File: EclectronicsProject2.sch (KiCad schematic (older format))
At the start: 84 parts, among them J7 Barrel_Jack, U11 TPS62290DRVR, U8 TPS62290DRVR

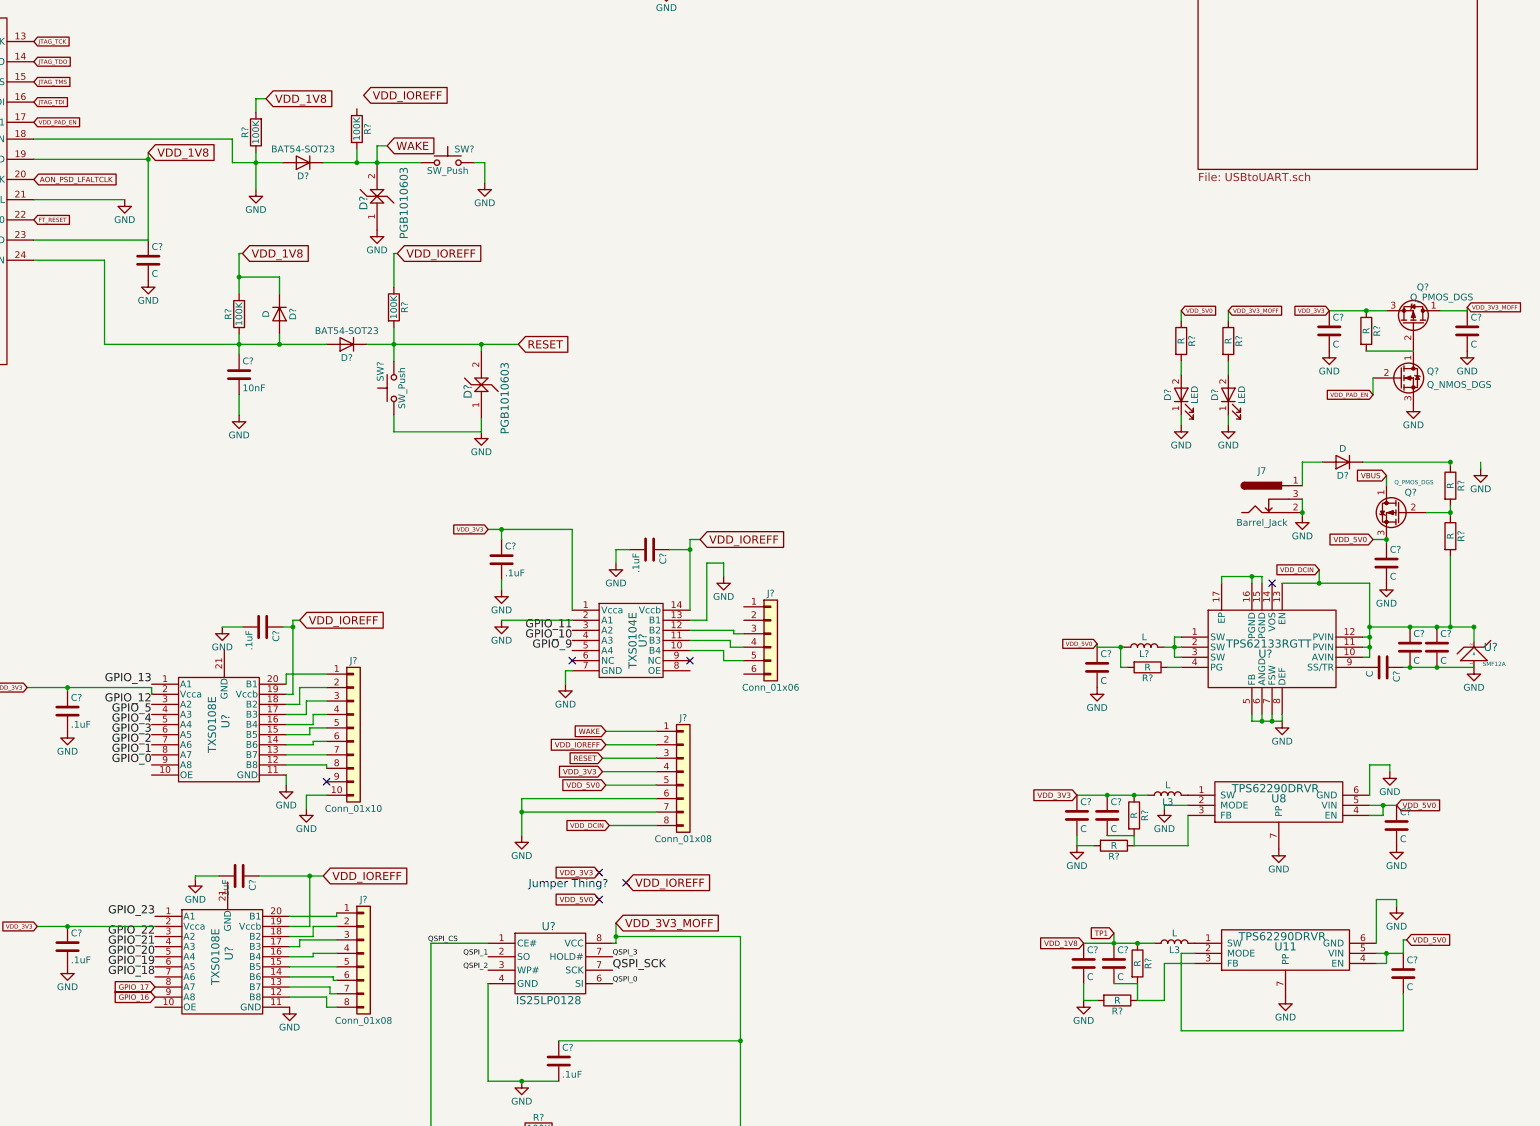
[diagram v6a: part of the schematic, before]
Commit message: adding some of the component labels
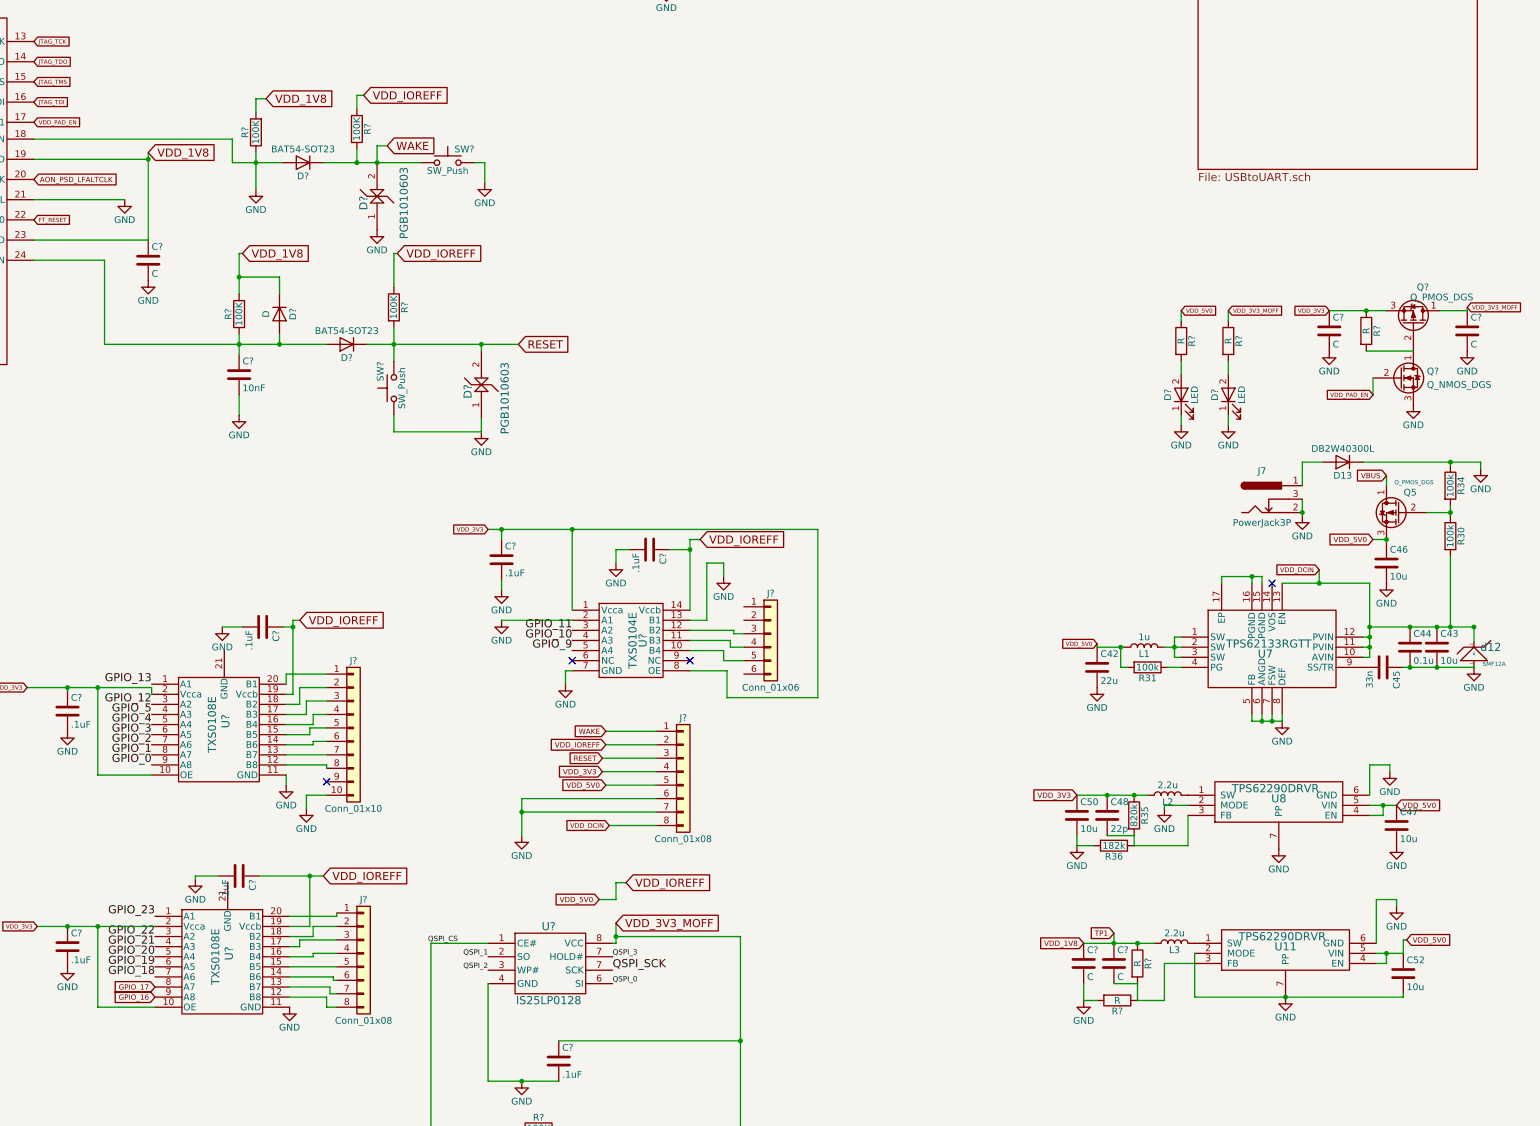
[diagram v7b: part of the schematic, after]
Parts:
- C42: renamed from C?; value C -> 22u
- C43, C46, C47, C50, C52: renamed from C?; value C -> 10u
- C44: renamed from C?; value C -> 0.1u
- C45: renamed from C?; value C -> 33n
- C48: renamed from C?; value C -> 22p
- D13: renamed from D?; value D -> DB2W40300L
- J7: value Barrel_Jack -> PowerJack3P
- L1: renamed from L?; value L -> 1u
- L2: renamed from L3; value L -> 2.2u
- L3: value L -> 2.2u
- R30, R31, R34: renamed from R?; value R -> 100k
- R35: renamed from R?; value R -> 820k
- R36: renamed from R?; value R -> 182k
- U7: renamed from U?; PART (none) -> 296-30225-1-ND
- gave numbers to parts that had none: 2
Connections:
- net VDD_IOREFF is gone; now on net VDD_5V0: C?.1, C?.1, C?.1, J?.2 (Pin_2), R?.1, U?.14 (Vccb), U?.19 (Vccb), U?.19 (Vccb)
- net GND: now also C52.2, D13.1 (K), R34.1, U11.2 (MODE)
- net VDD_3V3: now also U?.10 (OE), U?.10 (OE), U?.8 (OE)
- net VDD_5V0: now also R?.1
- no-connect marks 8 -> 5
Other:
- note removed: "Jumper Thing?\n"
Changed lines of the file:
@@
 IVDD
 $Comp
-L C C?
+L C C52
 U 1 1 59CDA679
 P 15725 8800
-F 0 "C?" H 15750 8900 50  0000 L CNN
-F 1 "C" H 15750 8700 50  0000 L CNN
+F 0 "C52" H 15750 8900 50  0000 L CNN
+F 1 "10u" H 15750 8700 50  0000 L CNN
 F 2 "" H 15763 8650 50  0001 C CNN
 F 3 "" H 15725 8800 50  0001 C CNN
@@
 P 14025 8575
 F 0 "L3" V 13975 8575 50  0000 C CNN
-F 1 "L" V 14100 8575 50  0000 C CNN
+F 1 "2.2u" V 14100 8575 50  0000 C CNN
 F 2 "" H 14025 8575 50  0001 C CNN
 F 3 "" H 14025 8575 50  0001 C CNN
@@
 $Comp
 L GND #PWR?
-U 1 1 59CE4525
-P 14850 8975
-F 0 "#PWR?" H 14850 8725 50  0001 C CNN
-F 1 "GND" H 14850 8825 50  0000 C CNN
-F 2 "" H 14850 8975 50  0001 C CNN
-F 3 "" H 14850 8975 50  0001 C CNN
-	1    14850 8975
-	1    0    0    -1
-$EndComp
-$Comp
-L GND #PWR?
 U 1 1 59CE4599
 P 15675 8300
@@
 $EndComp
 $Comp
-L C C?
+L C C47
 U 1 1 59CE5977
 P 15675 7700
-F 0 "C?" H 15700 7800 50  0000 L CNN
-F 1 "C" H 15700 7600 50  0000 L CNN
+F 0 "C47" H 15700 7800 50  0000 L CNN
+F 1 "10u" H 15700 7600 50  0000 L CNN
 F 2 "" H 15713 7550 50  0001 C CNN
 F 3 "" H 15675 7700 50  0001 C CNN
@@
 $EndComp
 $Comp
-L L L3
+L L L2
 U 1 1 59CE66A1
 P 13975 7475
-F 0 "L3" V 13925 7475 50  0000 C CNN
-F 1 "L" V 14050 7475 50  0000 C CNN
+F 0 "L2" V 13925 7475 50  0000 C CNN
+F 1 "2.2u" V 14050 7475 50  0000 C CNN
 F 2 "" H 13975 7475 50  0001 C CNN
 F 3 "" H 13975 7475 50  0001 C CNN
@@
 $EndComp
 $Comp
-L R R?
+L R R35
 U 1 1 59CE674E
 P 13725 7625
-F 0 "R?" V 13805 7625 50  0000 C CNN
-F 1 "R" V 13725 7625 50  0000 C CNN
+F 0 "R35" V 13805 7625 50  0000 C CNN
+F 1 "820k" V 13725 7625 50  0000 C CNN
 F 2 "" V 13655 7625 50  0001 C CNN
 F 3 "" H 13725 7625 50  0001 C CNN
@@
 $EndComp
 $Comp
-L C C?
+L C C48
 U 1 1 59CE6957
 P 13525 7625
-F 0 "C?" H 13550 7725 50  0000 L CNN
-F 1 "C" H 13550 7525 50  0000 L CNN
+F 0 "C48" H 13550 7725 50  0000 L CNN
+F 1 "22p" H 13550 7525 50  0000 L CNN
 F 2 "" H 13563 7475 50  0001 C CNN
 F 3 "" H 13525 7625 50  0001 C CNN
@@
 $EndComp
 $Comp
-L C C?
+L C C50
 U 1 1 59CE6FC0
 P 13300 7625
-F 0 "C?" H 13325 7725 50  0000 L CNN
-F 1 "C" H 13325 7525 50  0000 L CNN
+F 0 "C50" H 13325 7725 50  0000 L CNN
+F 1 "10u" H 13325 7525 50  0000 L CNN
 F 2 "" H 13338 7475 50  0001 C CNN
 F 3 "" H 13300 7625 50  0001 C CNN
@@
 $EndComp
 $Comp
-L R R?
+L R R36
 U 1 1 59CE7280
 P 13575 7850
-F 0 "R?" V 13655 7850 50  0000 C CNN
-F 1 "R" V 13575 7850 50  0000 C CNN
+F 0 "R36" V 13655 7850 50  0000 C CNN
+F 1 "182k" V 13575 7850 50  0000 C CNN
 F 2 "" V 13505 7850 50  0001 C CNN
 F 3 "" H 13575 7850 50  0001 C CNN
@@
 TP1
 $Comp
-L TPS62133RGTT U?
+L TPS62133RGTT U7
 U 1 1 59CD9E4B
 P 14700 6475
-F 0 "U?" H 14700 6525 60  0000 C CNN
+F 0 "U7" H 14700 6525 60  0000 C CNN
 F 1 "TPS62133RGTT" H 14725 6600 60  0000 C CNN
 F 2 "" H 14700 6475 60  0001 C CNN
 F 3 "" H 14700 6475 60  0001 C CNN
+F 4 "296-30225-1-ND" H 14700 6475 60  0001 C CNN "PART"
 	1    14700 6475
 	1    0    0    -1
@@
 $EndComp
 $Comp
-L C C?
+L C C45
 U 1 1 59CDAB83
 P 15575 6525
-F 0 "C?" H 15600 6625 50  0000 L CNN
-F 1 "C" H 15600 6425 50  0000 L CNN
+F 0 "C45" H 15600 6625 50  0000 L CNN
+F 1 "33n" H 15600 6425 50  0000 L CNN
 F 2 "" H 15613 6375 50  0001 C CNN
 F 3 "" H 15575 6525 50  0001 C CNN
@@
 $EndComp
 $Comp
-L C C?
+L C C44
 U 1 1 59CDAC24
 P 15775 6375
-F 0 "C?" H 15800 6475 50  0000 L CNN
-F 1 "C" H 15800 6275 50  0000 L CNN
+F 0 "C44" H 15800 6475 50  0000 L CNN
+F 1 "0.1u" H 15800 6275 50  0000 L CNN
 F 2 "" H 15813 6225 50  0001 C CNN
 F 3 "" H 15775 6375 50  0001 C CNN
@@
 $EndComp
 $Comp
-L C C?
+L C C43
 U 1 1 59CDACF5
 P 15975 6375
-F 0 "C?" H 16000 6475 50  0000 L CNN
-F 1 "C" H 16000 6275 50  0000 L CNN
+F 0 "C43" H 16000 6475 50  0000 L CNN
+F 1 "10u" H 16000 6275 50  0000 L CNN
 F 2 "" H 16013 6225 50  0001 C CNN
 F 3 "" H 15975 6375 50  0001 C CNN
@@
 $EndComp
 $Comp
-L SMF12A U?
+L SMF12A d12
 U 1 1 59CDB688
 P 16350 6425
-F 0 "U?" H 16375 6475 60  0000 C CNN
+F 0 "d12" H 16375 6475 60  0000 C CNN
 F 1 "SMF12A" H 16400 6350 31  0000 C CNN
 F 2 "" H 16150 6375 60  0001 C CNN
@@
 $EndComp
 $Comp
-L R R?
+L R R30
 U 1 1 59CDE56A
 P 16075 5550
-F 0 "R?" V 16155 5550 50  0000 C CNN
-F 1 "R" V 16075 5550 50  0000 C CNN
+F 0 "R30" V 16155 5550 50  0000 C CNN
+F 1 "100k" V 16075 5550 50  0000 C CNN
 F 2 "" V 16005 5550 50  0001 C CNN
 F 3 "" H 16075 5550 50  0001 C CNN
@@
 $EndComp
 $Comp
-L R R?
+L R R34
 U 1 1 59CDE6A4
 P 16075 5175
-F 0 "R?" V 16155 5175 50  0000 C CNN
-F 1 "R" V 16075 5175 50  0000 C CNN
+F 0 "R34" V 16155 5175 50  0000 C CNN
+F 1 "100k" V 16075 5175 50  0000 C CNN
 F 2 "" V 16005 5175 50  0001 C CNN
 F 3 "" H 16075 5175 50  0001 C CNN
@@
 $EndComp
 $Comp
-L Q_PMOS_DGS Q?
+L Q_PMOS_DGS Q5
 U 1 1 59CDFA93
 P 15700 5375
-F 0 "Q?" H 15575 5525 50  0000 L CNN
+F 0 "Q5" H 15575 5525 50  0000 L CNN
 F 1 "Q_PMOS_DGS" H 15450 5600 31  0000 L CNN
 F 2 "" H 15900 5475 50  0001 C CNN
@@
 $EndComp
 $Comp
-L C C?
+L C C46
 U 1 1 59CE0B13
 P 15600 5750
-F 0 "C?" H 15625 5850 50  0000 L CNN
-F 1 "C" H 15625 5650 50  0000 L CNN
+F 0 "C46" H 15625 5850 50  0000 L CNN
+F 1 "10u" H 15625 5650 50  0000 L CNN
 F 2 "" H 15638 5600 50  0001 C CNN
 F 3 "" H 15600 5750 50  0001 C CNN
@@
 P 14675 5275
 F 0 "J7" H 14675 5485 50  0000 C CNN
-F 1 "Barrel_Jack" H 14675 5100 50  0000 C CNN
+F 1 "PowerJack3P" H 14675 5100 50  0000 C CNN
 F 2 "" H 14725 5235 50  0001 C CNN
 F 3 "" H 14725 5235 50  0001 C CNN
@@
 $EndComp
 $Comp
-L L L?
+L L L1
 U 1 1 59CF21B5
 P 13800 6375
-F 0 "L?" V 13750 6375 50  0000 C CNN
-F 1 "L" V 13875 6375 50  0000 C CNN
+F 0 "L1" V 13750 6375 50  0000 C CNN
+F 1 "1u" V 13875 6375 50  0000 C CNN
 F 2 "" H 13800 6375 50  0001 C CNN
 F 3 "" H 13800 6375 50  0001 C CNN
@@
 $EndComp
 $Comp
-L R R?
-U 1 1 59CF2367
-P 13825 6525
-F 0 "R?" V 13905 6525 50  0000 C CNN
-F 1 "R" V 13825 6525 50  0000 C CNN
-F 2 "" V 13755 6525 50  0001 C CNN
-F 3 "" H 13825 6525 50  0001 C CNN
-	1    13825 6525
-	0    1    1    0
-$EndComp
-$Comp
-L C C?
+L C C42
 U 1 1 59CF2896
 P 13450 6525
-F 0 "C?" H 13475 6625 50  0000 L CNN
-F 1 "C" H 13475 6425 50  0000 L CNN
+F 0 "C42" H 13475 6625 50  0000 L CNN
+F 1 "22u" H 13475 6425 50  0000 L CNN
 F 2 "" H 13488 6375 50  0001 C CNN
 F 3 "" H 13450 6525 50  0001 C CNN
@@
 VDD_DCIN
 $Comp
-L D D?
+L D D13
 U 1 1 59CE7139
 P 15275 5000
-F 0 "D?" H 15275 5100 50  0000 C CNN
-F 1 "D" H 15275 4900 50  0000 C CNN
+F 0 "D13" H 15275 5100 50  0000 C CNN
+F 1 "DB2W40300L" H 15275 4900 50  0000 C CNN
 F 2 "" H 15275 5000 50  0001 C CNN
 F 3 "" H 15275 5000 50  0001 C CNN
@@
 	14175 8725 13950 8725
 Wire Wire Line
-	15725 9225 15725 8950
-Wire Wire Line
-	14075 9225 15725 9225
-Wire Wire Line
-	14075 8650 14075 9225
-Wire Wire Line
-	14175 8650 14075 8650
-Wire Wire Line
 	13300 7850 13300 7775
 Wire Wire Line
@@
 Connection ~ 14025 6375
 Wire Wire Line
-	14075 6525 13975 6525
-Wire Wire Line
 	13450 6375 13650 6375
-Wire Wire Line
-	13675 6525 13625 6525
-Wire Wire Line
-	13625 6525 13625 6375
 Connection ~ 13625 6375
 Wire Wire Line
@@
 	15500 4375 15500 4500
 Wire Wire Line
-	16075 5000 15425 5000
+	15425 5000 16300 5000
 Wire Wire Line
 	15125 5000 14975 5000
@@
 	9025 6175 9550 6175
 Wire Wire Line
-	8925 5500 9550 5500
+	8925 5500 11375 5500
 Wire Wire Line
 	9025 5500 9025 5575
@@
 Text GLabel 9750 8250 0    39   Input ~ 0
 VDD_5V0
-Text GLabel 9750 8050 0    39   Input ~ 0
-VDD_3V3
 Text GLabel 9950 8125 2    60   Input ~ 0
 VDD_IOREFF
-NoConn ~ 9750 8050
-NoConn ~ 9950 8125
-NoConn ~ 9750 8250
-Text Notes 9225 8175 0    60   ~ 0
-Jumper Thing?\n
 $Comp
 L IS25LP0128 U?
@@
 Wire Wire Line
 	2325 8850 2075 8850
+Wire Wire Line
+	10425 6550 10700 6550
+Wire Wire Line
+	10700 6550 10700 6750
+Wire Wire Line
+	10700 6750 11375 6750
+Wire Wire Line
+	11375 6750 11375 5500
+Connection ~ 9550 5500
+Wire Wire Line
+	6425 7325 6025 7325
+Wire Wire Line
+	6025 7325 6025 6675
+Connection ~ 6025 6675
+Wire Wire Line
+	6450 9050 6025 9050
+Wire Wire Line
+	6025 9050 6025 8450
+Connection ~ 6025 8450
+Wire Wire Line
+	9750 8250 9875 8250
+Wire Wire Line
+	9875 8250 9875 8125
+Wire Wire Line
+	9875 8125 9950 8125
+Wire Wire Line
+	8000 2275 7950 2275
+Wire Wire Line
+	7950 2275 7950 2375
+Wire Wire Line
+	14075 6525 13975 6525
+Wire Wire Line
+	13625 6525 13625 6375
+Wire Wire Line
+	13675 6525 13625 6525
+$Comp
+L R R31
+U 1 1 59CF2367
+P 13825 6525
+F 0 "R31" V 13905 6525 50  0000 C CNN
+F 1 "100k" V 13825 6525 50  0000 C CNN
+F 2 "" V 13755 6525 50  0001 C CNN
+F 3 "" H 13825 6525 50  0001 C CNN
+	1    13825 6525
+	0    1    1    0
+$EndComp
+Wire Wire Line
+	15725 8975 15725 8950
+Wire Wire Line
+	14175 8975 15725 8975
+Wire Wire Line
+	14175 8650 14175 8975
+Connection ~ 14850 8975
+$Comp
+L GND #PWR?
+U 1 1 59D03FF3
+P 14850 8975
+F 0 "#PWR?" H 14850 8725 50  0001 C CNN
+F 1 "GND" H 14850 8825 50  0000 C CNN
+F 2 "" H 14850 8975 50  0001 C CNN
+F 3 "" H 14850 8975 50  0001 C CNN
+	1    14850 8975
+	1    0    0    -1
+$EndComp
 $EndSCHEMATC

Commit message: updated values and part numbers
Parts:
- removed U? (x2): TXS0108E, symbol TXS0108E
- added C12, C13: 12p, symbol C
- added U2, U3: TXS0108E, symbol TXS0108E
- added Y1: clock, symbol clock
- C49, C51: renamed from C?; value C -> 1u
- C5: renamed from C?; value C -> 0.1u
- C54: renamed from C?; value C -> 22p
- C55: renamed from C?; value C -> 10u
- D3: renamed from D?; value D -> Diode
- R27, R28: renamed from R?; value R -> 330R
- R37: renamed from R?; value R -> 360k
- R39: renamed from R?; value R -> 180k
- R9: renamed from R?; value R -> 100k
- U11, U8: Part (none) -> 296-27030-1-ND
- U4: renamed from U?; Part (none) -> 296-20698-1-ND
- gave numbers to parts that had none: 33
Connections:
- net GND: now also U7.15 (PGND), U7.16 (PGND), U7.17 (EP), C12.2, C13.2, U2.21 (GND), U3.11 (GND), U3.21 (GND), Y1.2 (GND), Y1.4 (GND); no longer C43.2, C44.2, C45.1, D13.1 (K), d12.1 (In)
- net GPIO_0: now also U3.9 (A8)
- net GPIO_1: now also U3.8 (A7)
- net GPIO_12: now also U3.3 (A2)
- net GPIO_13: now also U3.1 (A1)
- net GPIO_16: now also U2.9 (A8)
- net GPIO_17: now also U2.8 (A7)
- net GPIO_18: now also U2.7 (A6)
- net GPIO_19: now also U2.6 (A5)
- net GPIO_2: now also U3.7 (A6)
- net GPIO_20: now also U2.5 (A4)
- net GPIO_21: now also U2.4 (A3)
- net GPIO_22: now also U2.3 (A2)
- net GPIO_23: now also U2.1 (A1)
- net GPIO_3: now also U3.6 (A5)
- net GPIO_4: now also U3.5 (A4)
- net GPIO_5: now also U3.4 (A3)
- net VDD_3V3: now also U2.10 (OE), U2.2 (Vcca), U3.10 (OE), U3.2 (Vcca)
- net VDD_5V0: now also U7.14 (VOS), U2.19 (Vccb), U3.19 (Vccb)
- net VDD_DCIN: now also D13.1 (K)
- net at U1A.10 (XTAL_XO): now also C13.1, Y1.3
- net at U1A.9 (XTAL_XI): now also C12.1, Y1.1
- net DCIN_DET: now reaches Q5.2 (G), R30.1, R34.2
- net at J3.1 (Pin_1): now also U3.20 (B1)
- net at J3.2 (Pin_2): now also U3.18 (B2)
- net at J3.3 (Pin_3): now also U3.17 (B3)
- net at J3.4 (Pin_4): now also U3.16 (B4)
- net at J3.5 (Pin_5): now also U3.15 (B5)
- net at J3.6 (Pin_6): now also U3.14 (B6)
- net at J3.7 (Pin_7): now also U3.13 (B7)
- net at J3.8 (Pin_8): now also U3.12 (B8)
- net at J2.8 (Pin_8): now also U2.12 (B8)
- net at J2.7 (Pin_7): now also U2.13 (B7)
- net at J2.6 (Pin_6): now also U2.14 (B6)
- net at J2.5 (Pin_5): now also U2.15 (B5)
- net at J2.4 (Pin_4): now also U2.16 (B4)
- net at J2.3 (Pin_3): now also U2.17 (B3)
- net at J2.2 (Pin_2): now also U2.18 (B2)
- net at J2.1 (Pin_1): now also U2.20 (B1)
- new net: C43.2, C44.2, C45.1, d12.1 (In)
- no-connect marks 5 -> 4
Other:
- note added: "Bluetooth Module"
- note added: "Clock\n"
- note added: "Honestly no idea"
- note added: "LEDs"
- note added: "Logic Level Shifters\n"
- note added: "Memory"
- note added: "Voltage Regulators"
- moved on the sheet: C10, C11, C18, C19, C20, C21, C22, C23, C4, C42, C43, C44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
